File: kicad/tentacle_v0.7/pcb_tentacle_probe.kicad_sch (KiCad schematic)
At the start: 29 parts, among them J1501 Conn_02x20, J1502 Conn_01x12, U1501 RP2040, U1502 W25Q32JVS, U1503 TXB0108PW, U1504 TXB0108PW

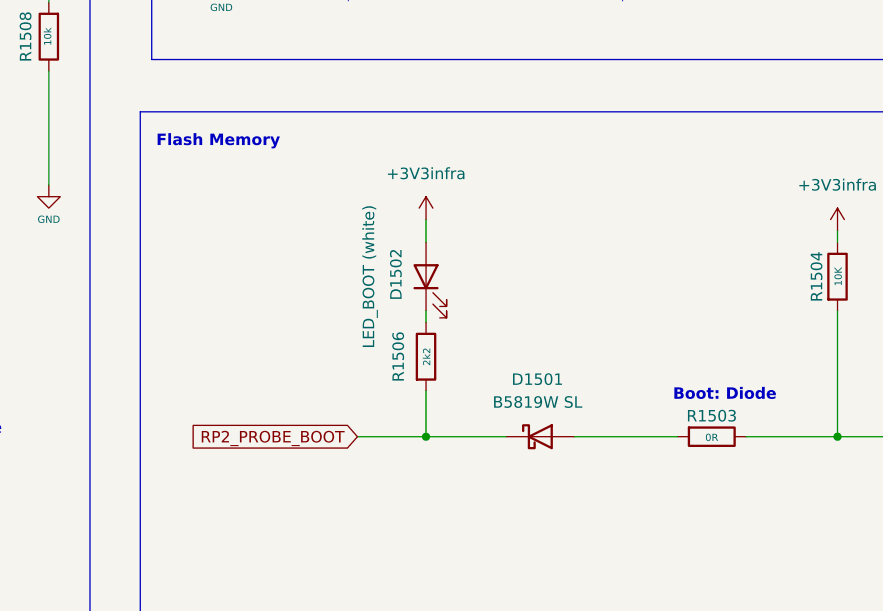
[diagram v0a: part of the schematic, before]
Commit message: Tentacle v0.7: Fix LEDs. Import new symbols and footprints
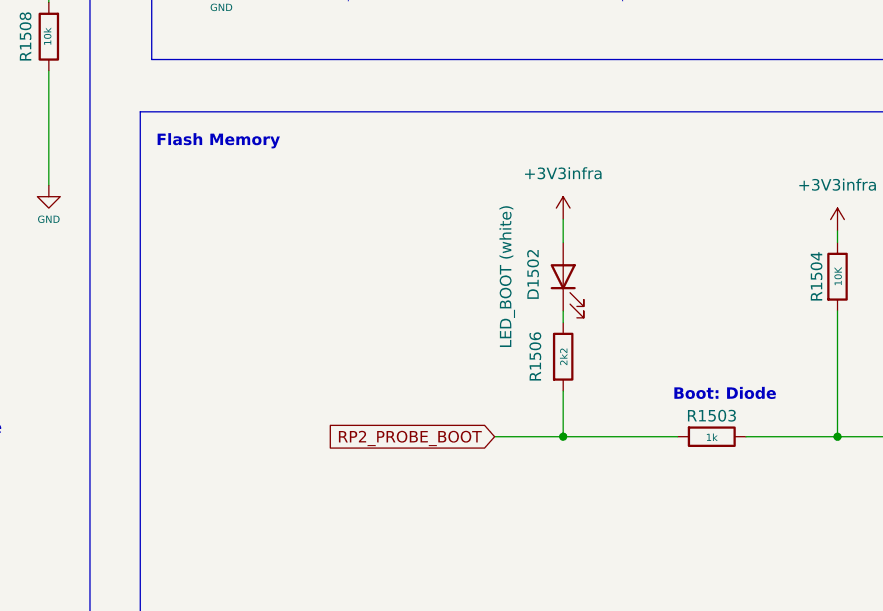
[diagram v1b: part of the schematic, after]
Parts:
- removed D1501: B5819W SL, Diode_SMD:D_SOD-123, symbol Device:D_Schottky
- D1502, D1503: footprint 00_project_library:LED_0603_1608Metric -> LED_SMD:LED_0805_2012Metric; JLC C2290 -> C34499
- R1503: value 0R -> 1k
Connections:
- net RP2_PROBE_BOOT: now also R1503.2
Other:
- moved on the sheet: D1502, R1506
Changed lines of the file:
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@@
 	)
 	(junction
-		(at 179.07 95.25)
+		(at 194.31 95.25)
 		(diameter 0)
 		(color 0 0 0 0)
@@
 	(wire
 		(pts
+			(xy 214.63 95.25) (xy 224.79 95.25)
+		)
+		(stroke
+			(width 0)
+			(type default)
+		)
+	)
+	(wire
+		(pts
 			(xy 68.58 34.29) (xy 68.58 31.75)
 		)
@@
 	(wire
 		(pts
-			(xy 179.07 81.28) (xy 179.07 82.55)
+			(xy 194.31 81.28) (xy 194.31 82.55)
 		)
 		(stroke
@@
 	(wire
 		(pts
-			(xy 195.58 95.25) (xy 207.01 95.25)
-		)
-		(stroke
-			(width 0)
-			(type default)
-		)
-	)
-	(wire
-		(pts
 			(xy 81.28 34.29) (xy 81.28 31.75)
 		)
@@
 	(wire
 		(pts
-			(xy 171.45 95.25) (xy 179.07 95.25)
+			(xy 186.69 95.25) (xy 194.31 95.25)
 		)
 		(stroke
@@
 	(wire
 		(pts
-			(xy 179.07 90.17) (xy 179.07 95.25)
+			(xy 194.31 90.17) (xy 194.31 95.25)
 		)
 		(stroke
@@
 	(wire
 		(pts
-			(xy 179.07 95.25) (xy 187.96 95.25)
+			(xy 194.31 95.25) (xy 207.01 95.25)
 		)
 		(stroke
@@
 	(wire
 		(pts
-			(xy 214.63 95.25) (xy 224.79 95.25)
-		)
-		(stroke
-			(width 0)
-			(type default)
-		)
-	)
-	(wire
-		(pts
 			(xy 233.68 40.64) (xy 233.68 41.91)
 		)
@@
 	(wire
 		(pts
-			(xy 179.07 71.12) (xy 179.07 73.66)
+			(xy 194.31 71.12) (xy 194.31 73.66)
 		)
 		(stroke
@@
 	(global_label "RP2_PROBE_BOOT"
 		(shape input)
-		(at 171.45 95.25 180)
+		(at 186.69 95.25 180)
 		(fields_autoplaced yes)
 		(effects
@@
 		)
 		(property "Intersheetrefs" "${INTERSHEET_REFS}"
-			(at 151.4969 95.25 0)
+			(at 166.7369 95.25 0)
 			(effects
 				(font
@@
 	(symbol
 		(lib_id "00_project_library:+3V3infra")
-		(at 179.07 71.12 0)
+		(at 194.31 71.12 0)
 		(unit 1)
 		(exclude_from_sim no)
@@
 		(fields_autoplaced yes)
 		(property "Reference" "#PWR0238"
-			(at 179.07 74.93 0)
+			(at 194.31 74.93 0)
 			(effects
 				(font
@@
 		)
 		(property "Value" "+3V3infra"
-			(at 179.07 66.04 0)
+			(at 194.31 66.04 0)
 			(effects
 				(font
@@
 		)
 		(property "Footprint" ""
-			(at 179.07 71.12 0)
+			(at 194.31 71.12 0)
 			(effects
 				(font
@@
 		)
 		(property "Datasheet" ""
-			(at 179.07 71.12 0)
+			(at 194.31 71.12 0)
 			(effects
 				(font
@@
 		)
 		(property "Description" "Power symbol creates a global label with name \"+3V3infra\""
-			(at 179.07 71.12 0)
+			(at 194.31 71.12 0)
 			(effects
 				(font
@@
 			)
 		)
-		(property "Footprint" "00_project_library:LED_0603_1608Metric"
+		(property "Footprint" "LED_SMD:LED_0805_2012Metric"
 			(at 128.27 60.96 0)
 			(effects
@@
 			)
 		)
-		(property "Description" ""
+		(property "Description" "Light emitting diode"
 			(at 128.27 60.96 0)
 			(effects
@@
 			)
 		)
-		(property "JLC" "C2290"
+		(property "JLC" "C34499"
 			(at 128.27 60.96 0)
 			(effects
@@
 	)
 	(symbol
-		(lib_id "Device:D_Schottky")
-		(at 191.77 95.25 0)
-		(unit 1)
-		(exclude_from_sim no)
-		(in_bom yes)
-		(on_board yes)
-		(dnp no)
-		(property "Reference" "D1501"
-			(at 191.4525 88.9 0)
-			(effects
-				(font
-					(size 1.27 1.27)
-				)
-			)
-		)
-		(property "Value" "B5819W SL"
-			(at 191.4525 91.44 0)
-			(effects
-				(font
-					(size 1.27 1.27)
-				)
-			)
-		)
-		(property "Footprint" "Diode_SMD:D_SOD-123"
-			(at 191.77 95.25 0)
-			(effects
-				(font
-					(size 1.27 1.27)
-				)
-				(hide yes)
-			)
-		)
-		(property "Datasheet" "https://datasheet.lcsc.com/lcsc/2304140030_Jiangsu-Changjing-Electronics-Technology-Co---Ltd--B5819W-SL_C8598.pdf"
-			(at 191.77 95.25 0)
-			(effects
-				(font
-					(size 1.27 1.27)
-				)
-				(hide yes)
-			)
-		)
-		(property "Description" ""
-			(at 191.77 95.25 0)
-			(effects
-				(font
-					(size 1.27 1.27)
-				)
-				(hide yes)
-			)
-		)
-		(property "JLC" "C8598"
-			(at 191.77 95.25 0)
-			(effects
-				(font
-					(size 1.27 1.27)
-				)
-				(hide yes)
-			)
-		)
-		(pin "1"
-		)
-		(pin "2"
-		)
-		(instances
-			(project "pcb_tentacle"
-				(path "/35c47459-45a7-4753-acae-c8b47e7575e1/cd9bbde0-3ad0-43d1-a674-4a86d38bbcb3"
-					(reference "D1501")
-					(unit 1)
-				)
-			)
-		)
-	)
-	(symbol
 		(lib_id "00_project_library:W25Q32JVS")
 		(at 262.89 102.87 0)
@@
 			)
 		)
-		(property "Value" "0R"
+		(property "Value" "1k"
 			(at 210.82 95.3516 90)
 			(effects
@@
 	(symbol
 		(lib_id "Device:R")
-		(at 179.07 86.36 0)
+		(at 194.31 86.36 0)
 		(unit 1)
 		(exclude_from_sim no)
@@
 		(dnp no)
 		(property "Reference" "R1506"
-			(at 176.022 86.36 90)
+			(at 191.262 86.36 90)
 			(effects
 				(font
@@
 		)
 		(property "Value" "2k2"
-			(at 179.1716 86.36 90)
+			(at 194.4116 86.36 90)
 			(effects
 				(font
@@
 		)
 		(property "Footprint" "Resistor_SMD:R_0402_1005Metric"
-			(at 177.292 86.36 90)
+			(at 192.532 86.36 90)
 			(effects
 				(font
@@
 		)
 		(property "Datasheet" "~"
-			(at 179.07 86.36 0)
+			(at 194.31 86.36 0)
 			(effects
 				(font
@@
 		)
 		(property "Description" ""
-			(at 179.07 86.36 0)
+			(at 194.31 86.36 0)
 			(effects
 				(font
@@
 	(symbol
 		(lib_id "00_project_library:LED WHITE")
-		(at 179.07 77.47 90)
+		(at 194.31 77.47 90)
 		(unit 1)
 		(exclude_from_sim no)
@@
 		(dnp no)
 		(property "Reference" "D1502"
-			(at 175.768 77.216 0)
+			(at 191.008 77.216 0)
 			(effects
 				(font
@@
 		)
 		(property "Value" "white"
-			(at 175.26 79.0575 0)
+			(at 190.5 79.0575 0)
 			(effects
 				(font
@@
 			)
 		)
-		(property "Footprint" "00_project_library:LED_0603_1608Metric"
-			(at 179.07 77.47 0)
+		(property "Footprint" "LED_SMD:LED_0805_2012Metric"
+			(at 194.31 77.47 0)
 			(effects
 				(font
@@
 		)
 		(property "Datasheet" "~"
-			(at 179.07 77.47 0)
+			(at 194.31 77.47 0)
 			(effects
 				(font
@@
 			)
 		)
-		(property "Description" ""
-			(at 179.07 77.47 0)
+		(property "Description" "Light emitting diode"
+			(at 194.31 77.47 0)
 			(effects
 				(font
@@
 			)
 		)
-		(property "JLC" "C2290"
-			(at 179.07 77.47 0)
+		(property "JLC" "C34499"
+			(at 194.31 77.47 0)
 			(effects
 				(font
@@
 		)
 		(property "Label" "LED_BOOT (white)"
-			(at 172.72 77.47 0)
+			(at 187.96 77.47 0)
 			(effects
 				(font
